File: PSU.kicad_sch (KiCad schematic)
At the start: 34 parts

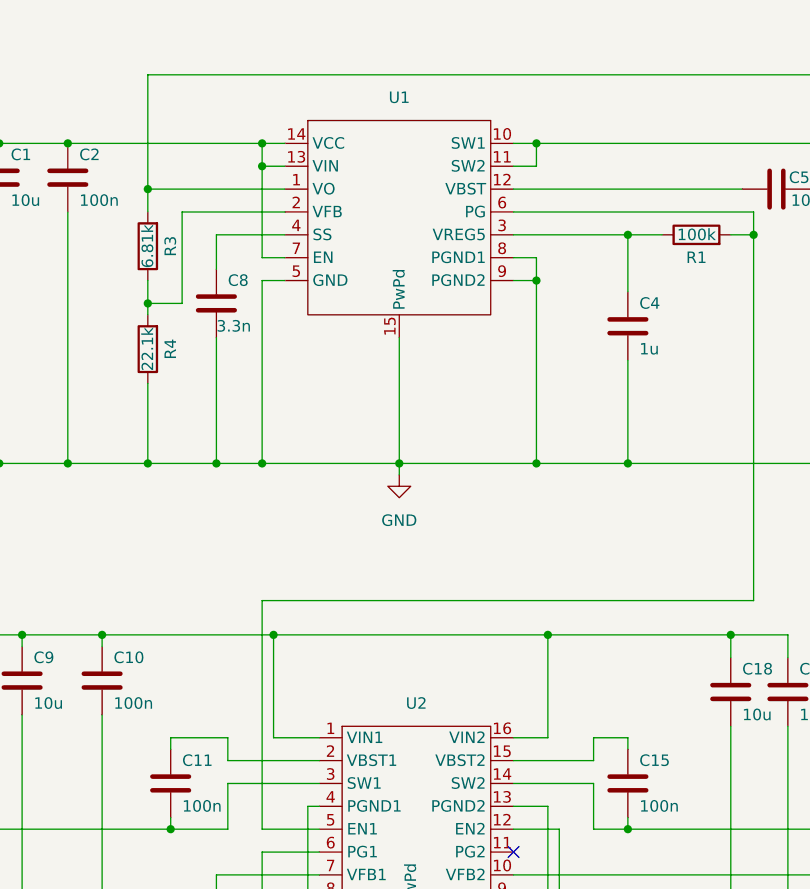
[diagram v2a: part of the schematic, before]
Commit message: Now follows with Electrical Rules
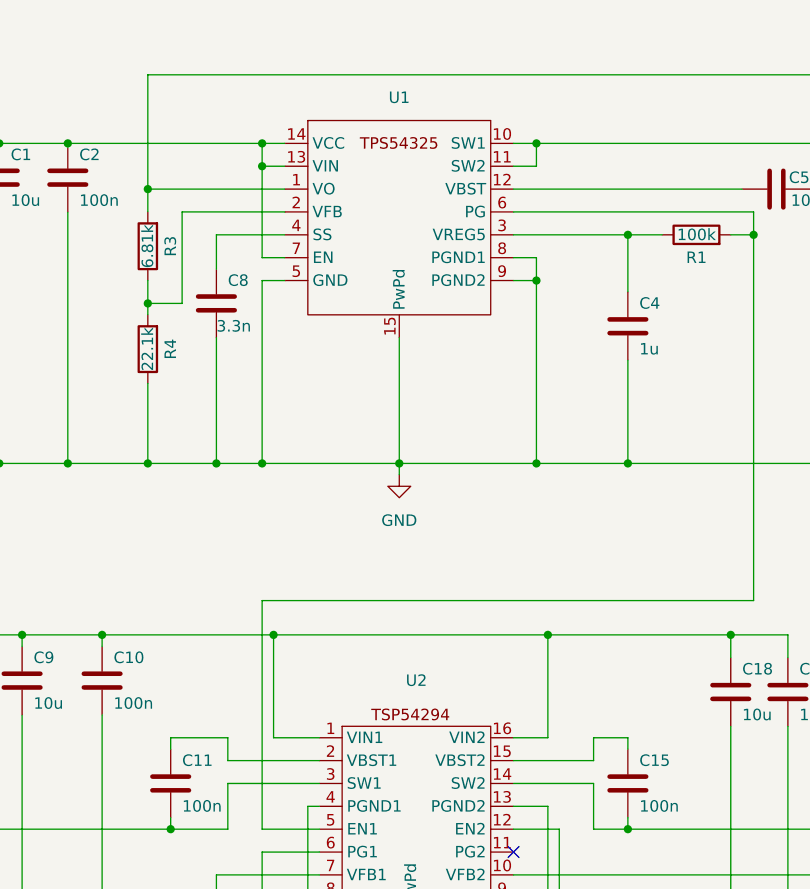
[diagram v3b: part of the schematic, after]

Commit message: Added footprints to symbols
Some nice light work
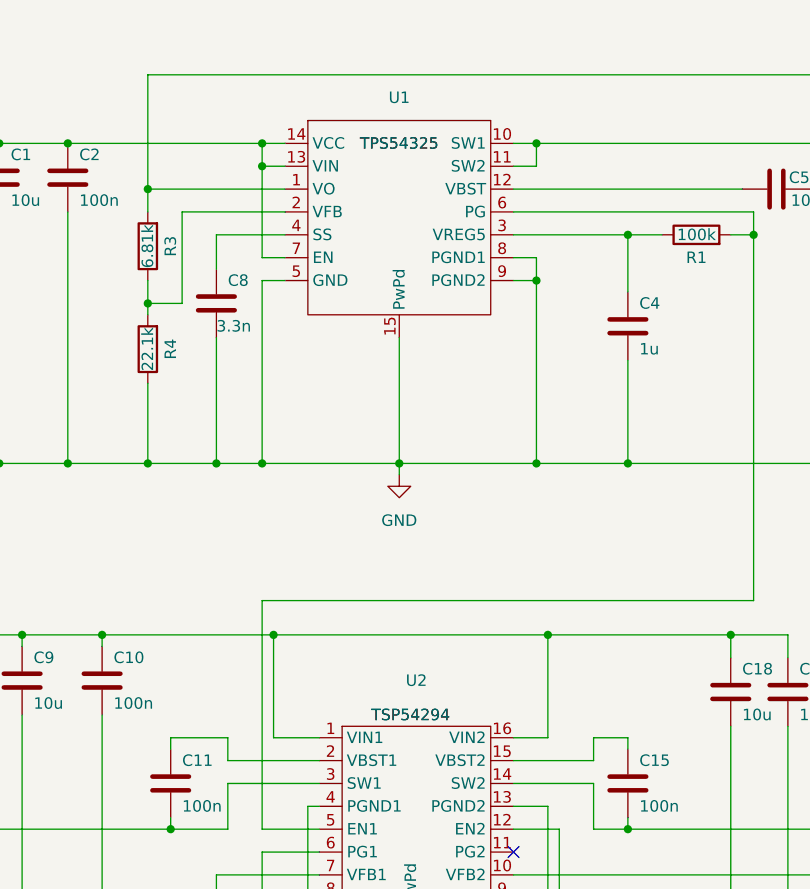
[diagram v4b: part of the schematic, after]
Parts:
- C1, C10, C11, C12, C13, C14, C15, C16, C17, C18, C19, C2, C3, C4, C5, C6, C7, C8, C9: footprint (none) -> Capacitor_SMD:C_1206_3216Metric
- FB1: footprint (none) -> Inductor_SMD:L_0603_1608Metric
- L1, L2, L3: footprint (none) -> Inductor_SMD:L_0805_2012Metric
- R1, R2, R3, R4, R5, R6, R7, R8, R9: footprint (none) -> Resistor_SMD:R_1206_3216Metric
- U1: value ~ -> TPS54325; footprint (none) -> Package_SO:TSSOP-14-1EP_4.4x5mm_P0.65mm
- U2: value ~ -> TSP54294; footprint (none) -> Package_SO:HTSSOP-16-1EP_4.4x5mm_P0.65mm_EP3x3mm
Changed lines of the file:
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@@
       (effects (font (size 1.27 1.27)))
     )
-    (property "Footprint" "" (at 101.6 130.81 0)
+    (property "Footprint" "Inductor_SMD:L_0805_2012Metric" (at 101.6 130.81 0)
       (effects (font (size 1.27 1.27)) hide)
     )
@@
       (effects (font (size 1.27 1.27)) (justify left))
     )
-    (property "Footprint" "" (at 180.0352 129.54 0)
+    (property "Footprint" "Capacitor_SMD:C_1206_3216Metric" (at 180.0352 129.54 0)
       (effects (font (size 1.27 1.27)) hide)
     )
@@
       (effects (font (size 1.27 1.27)))
     )
-    (property "Footprint" "" (at 237.998 146.05 90)
+    (property "Footprint" "Resistor_SMD:R_1206_3216Metric" (at 237.998 146.05 90)
       (effects (font (size 1.27 1.27)) hide)
     )
@@
       (effects (font (size 1.27 1.27)) (justify left))
     )
-    (property "Footprint" "" (at 93.6752 139.7 0)
+    (property "Footprint" "Capacitor_SMD:C_1206_3216Metric" (at 93.6752 139.7 0)
       (effects (font (size 1.27 1.27)) hide)
     )
@@
       (effects (font (size 1.27 1.27)) (justify left))
     )
-    (property "Footprint" "" (at 216.8652 66.04 0)
+    (property "Footprint" "Capacitor_SMD:C_1206_3216Metric" (at 216.8652 66.04 0)
       (effects (font (size 1.27 1.27)) hide)
     )
@@
       (effects (font (size 1.27 1.27)) (justify left))
     )
-    (property "Footprint" "" (at 227.0252 139.7 0)
+    (property "Footprint" "Capacitor_SMD:C_1206_3216Metric" (at 227.0252 139.7 0)
       (effects (font (size 1.27 1.27)) hide)
     )
@@
       (effects (font (size 1.27 1.27)) (justify left))
     )
-    (property "Footprint" "" (at 134.3152 76.2 0)
+    (property "Footprint" "Capacitor_SMD:C_1206_3216Metric" (at 134.3152 76.2 0)
       (effects (font (size 1.27 1.27)) hide)
     )
@@
       (effects (font (size 1.27 1.27)) (justify left))
     )
-    (property "Footprint" "" (at 191.4652 119.38 0)
+    (property "Footprint" "Capacitor_SMD:C_1206_3216Metric" (at 191.4652 119.38 0)
       (effects (font (size 1.27 1.27)) hide)
     )
@@
       (effects (font (size 1.27 1.27)))
     )
-    (property "Footprint" "" (at 237.998 135.89 90)
+    (property "Footprint" "Resistor_SMD:R_1206_3216Metric" (at 237.998 135.89 90)
       (effects (font (size 1.27 1.27)) hide)
     )
@@
       (effects (font (size 1.27 1.27)) (justify left))
     )
-    (property "Footprint" "" (at 180.0352 78.74 0)
+    (property "Footprint" "Capacitor_SMD:C_1206_3216Metric" (at 180.0352 78.74 0)
       (effects (font (size 1.27 1.27)) hide)
     )
@@
       (effects (font (size 1.27 1.27)))
     )
-    (property "Footprint" "" (at 127.508 77.47 90)
+    (property "Footprint" "Resistor_SMD:R_1206_3216Metric" (at 127.508 77.47 90)
       (effects (font (size 1.27 1.27)) hide)
     )
@@
       (effects (font (size 1.27 1.27)) (justify left))
     )
-    (property "Footprint" "" (at 117.8052 62.23 0)
+    (property "Footprint" "Capacitor_SMD:C_1206_3216Metric" (at 117.8052 62.23 0)
       (effects (font (size 1.27 1.27)) hide)
     )
@@
       (effects (font (size 1.27 1.27)) (justify left))
     )
-    (property "Footprint" "" (at 112.7252 118.11 0)
+    (property "Footprint" "Capacitor_SMD:C_1206_3216Metric" (at 112.7252 118.11 0)
       (effects (font (size 1.27 1.27)) hide)
     )
@@
       (effects (font (size 1.27 1.27)) (justify left))
     )
-    (property "Footprint" "" (at 129.2352 129.54 0)
+    (property "Footprint" "Capacitor_SMD:C_1206_3216Metric" (at 129.2352 129.54 0)
       (effects (font (size 1.27 1.27)) hide)
     )
@@
       (effects (font (size 1.27 1.27)))
     )
-    (property "Footprint" "" (at 208.28 54.61 0)
+    (property "Footprint" "Inductor_SMD:L_0805_2012Metric" (at 208.28 54.61 0)
       (effects (font (size 1.27 1.27)) hide)
     )
@@
   )
   (symbol (lib_id "GuitarZero:TPS54294") (at 154.94 129.54 0) (unit 1)
-    (in_bom yes) (on_board yes) (dnp no) (fields_autoplaced)
+    (in_bom yes) (on_board yes) (dnp no)
     (property "Reference" "U2" (at 155.575 114.3 0)
       (effects (font (size 1.27 1.27)))
     )
-    (property "Value" "~" (at 154.94 116.84 0)
-      (effects (font (size 1.27 1.27)))
-    )
-    (property "Footprint" "" (at 154.94 116.84 0)
+    (property "Value" "TSP54294" (at 154.94 118.11 0)
+      (effects (font (size 1.27 1.27)))
+    )
+    (property "Footprint" "Package_SO:HTSSOP-16-1EP_4.4x5mm_P0.65mm_EP3x3mm" (at 154.94 116.84 0)
       (effects (font (size 1.27 1.27)) hide)
     )
@@
       (effects (font (size 1.27 1.27)) (justify left))
     )
-    (property "Footprint" "" (at 219.4052 139.7 0)
+    (property "Footprint" "Capacitor_SMD:C_1206_3216Metric" (at 219.4052 139.7 0)
       (effects (font (size 1.27 1.27)) hide)
     )
@@
       (effects (font (size 1.27 1.27)))
     )
-    (property "Footprint" "" (at 186.69 66.548 90)
+    (property "Footprint" "Resistor_SMD:R_1206_3216Metric" (at 186.69 66.548 90)
       (effects (font (size 1.27 1.27)) hide)
     )
@@
       (effects (font (size 1.27 1.27)) (justify left))
     )
-    (property "Footprint" "" (at 121.6152 118.11 0)
+    (property "Footprint" "Capacitor_SMD:C_1206_3216Metric" (at 121.6152 118.11 0)
       (effects (font (size 1.27 1.27)) hide)
     )
@@
       (effects (font (size 1.27 1.27)) (justify left))
     )
-    (property "Footprint" "" (at 178.7652 147.32 0)
+    (property "Footprint" "Capacitor_SMD:C_1206_3216Metric" (at 178.7652 147.32 0)
       (effects (font (size 1.27 1.27)) hide)
     )
@@
   )
   (symbol (lib_id "GuitarZero:TPS54325") (at 153.67 62.23 0) (unit 1)
-    (in_bom yes) (on_board yes) (dnp no) (fields_autoplaced)
+    (in_bom yes) (on_board yes) (dnp no)
     (property "Reference" "U1" (at 153.67 49.53 0)
       (effects (font (size 1.27 1.27)))
     )
-    (property "Value" "~" (at 153.67 62.23 0)
-      (effects (font (size 1.27 1.27)))
-    )
-    (property "Footprint" "" (at 153.67 62.23 0)
+    (property "Value" "TPS54325" (at 153.67 54.61 0)
+      (effects (font (size 1.27 1.27)))
+    )
+    (property "Footprint" "Package_SO:TSSOP-14-1EP_4.4x5mm_P0.65mm" (at 153.67 62.23 0)
       (effects (font (size 1.27 1.27)) hide)
     )
@@
       (effects (font (size 1.27 1.27)))
     )
-    (property "Footprint" "" (at 72.898 146.05 90)
+    (property "Footprint" "Resistor_SMD:R_1206_3216Metric" (at 72.898 146.05 90)
       (effects (font (size 1.27 1.27)) hide)
     )
@@
       (effects (font (size 1.27 1.27)) (justify left))
     )
-    (property "Footprint" "" (at 101.6 58.42 0)
+    (property "Footprint" "Capacitor_SMD:C_1206_3216Metric" (at 101.6 58.42 0)
       (effects (font (size 1.27 1.27)) hide)
     )
@@
       (effects (font (size 1.27 1.27)) (justify left))
     )
-    (property "Footprint" "" (at 197.8152 119.38 0)
+    (property "Footprint" "Capacitor_SMD:C_1206_3216Metric" (at 197.8152 119.38 0)
       (effects (font (size 1.27 1.27)) hide)
     )
@@
       (effects (font (size 1.27 1.27)))
     )
-    (property "Footprint" "" (at 208.28 130.81 0)
+    (property "Footprint" "Inductor_SMD:L_0805_2012Metric" (at 208.28 130.81 0)
       (effects (font (size 1.27 1.27)) hide)
     )
@@
       (effects (font (size 1.27 1.27)) (justify left))
     )
-    (property "Footprint" "" (at 225.7552 66.04 0)
+    (property "Footprint" "Capacitor_SMD:C_1206_3216Metric" (at 225.7552 66.04 0)
       (effects (font (size 1.27 1.27)) hide)
     )
@@
       (effects (font (size 1.27 1.27)))
     )
-    (property "Footprint" "" (at 259.08 129.032 90)
+    (property "Footprint" "Resistor_SMD:R_1206_3216Metric" (at 259.08 129.032 90)
       (effects (font (size 1.27 1.27)) hide)
     )
@@
       (effects (font (size 1.27 1.27)))
     )
-    (property "Footprint" "" (at 251.46 132.588 90)
+    (property "Footprint" "Inductor_SMD:L_0603_1608Metric" (at 251.46 132.588 90)
       (effects (font (size 1.27 1.27)) hide)
     )
@@
       (effects (font (size 1.27 1.27)))
     )
-    (property "Footprint" "" (at 191.77 60.6552 0)
+    (property "Footprint" "Capacitor_SMD:C_1206_3216Metric" (at 191.77 60.6552 0)
       (effects (font (size 1.27 1.27)) hide)
     )
@@
       (effects (font (size 1.27 1.27)))
     )
-    (property "Footprint" "" (at 188.468 143.51 90)
+    (property "Footprint" "Resistor_SMD:R_1206_3216Metric" (at 188.468 143.51 90)
       (effects (font (size 1.27 1.27)) hide)
     )
@@
       (effects (font (size 1.27 1.27)))
     )
-    (property "Footprint" "" (at 72.898 135.89 90)
+    (property "Footprint" "Resistor_SMD:R_1206_3216Metric" (at 72.898 135.89 90)
       (effects (font (size 1.27 1.27)) hide)
     )
@@
       (effects (font (size 1.27 1.27)))
     )
-    (property "Footprint" "" (at 127.508 66.04 90)
+    (property "Footprint" "Resistor_SMD:R_1206_3216Metric" (at 127.508 66.04 90)
       (effects (font (size 1.27 1.27)) hide)
     )
@@
       (effects (font (size 1.27 1.27)) (justify left))
     )
-    (property "Footprint" "" (at 110.1852 62.23 0)
+    (property "Footprint" "Capacitor_SMD:C_1206_3216Metric" (at 110.1852 62.23 0)
       (effects (font (size 1.27 1.27)) hide)
     )
@@
       (effects (font (size 1.27 1.27)) (justify left))
     )
-    (property "Footprint" "" (at 83.5152 139.7 0)
-      (effects (font (size 1.27 1.27)) hide)
-    )
+    (property "Footprint" "Capacitor_SMD:C_1206_3216Metric" (at 83.5152 139.7 0)
+      (effects (font (size 1.27 1.27)) hide)
+    )

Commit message: Changed Reistor and Capacitor size fomr 1206 to 0805
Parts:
- C1, C10, C11, C12, C13, C14, C15, C16, C17, C18, C19, C2, C3, C4, C5, C6, C7, C8, C9: footprint Capacitor_SMD:C_1206_3216Metric -> Capacitor_SMD:C_0805_2012Metric
- R1, R2, R3, R4, R5, R6, R7, R8, R9: footprint Resistor_SMD:R_1206_3216Metric -> Resistor_SMD:R_0805_2012Metric
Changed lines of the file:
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@@
       (effects (font (size 1.27 1.27)) (justify left))
     )
-    (property "Footprint" "Capacitor_SMD:C_1206_3216Metric" (at 180.0352 129.54 0)
+    (property "Footprint" "Capacitor_SMD:C_0805_2012Metric" (at 180.0352 129.54 0)
       (effects (font (size 1.27 1.27)) hide)
     )
@@
       (effects (font (size 1.27 1.27)))
     )
-    (property "Footprint" "Resistor_SMD:R_1206_3216Metric" (at 237.998 146.05 90)
+    (property "Footprint" "Resistor_SMD:R_0805_2012Metric" (at 237.998 146.05 90)
       (effects (font (size 1.27 1.27)) hide)
     )
@@
       (effects (font (size 1.27 1.27)) (justify left))
     )
-    (property "Footprint" "Capacitor_SMD:C_1206_3216Metric" (at 93.6752 139.7 0)
+    (property "Footprint" "Capacitor_SMD:C_0805_2012Metric" (at 93.6752 139.7 0)
       (effects (font (size 1.27 1.27)) hide)
     )
@@
       (effects (font (size 1.27 1.27)) (justify left))
     )
-    (property "Footprint" "Capacitor_SMD:C_1206_3216Metric" (at 216.8652 66.04 0)
+    (property "Footprint" "Capacitor_SMD:C_0805_2012Metric" (at 216.8652 66.04 0)
       (effects (font (size 1.27 1.27)) hide)
     )
@@
       (effects (font (size 1.27 1.27)) (justify left))
     )
-    (property "Footprint" "Capacitor_SMD:C_1206_3216Metric" (at 227.0252 139.7 0)
+    (property "Footprint" "Capacitor_SMD:C_0805_2012Metric" (at 227.0252 139.7 0)
       (effects (font (size 1.27 1.27)) hide)
     )
@@
       (effects (font (size 1.27 1.27)) (justify left))
     )
-    (property "Footprint" "Capacitor_SMD:C_1206_3216Metric" (at 134.3152 76.2 0)
+    (property "Footprint" "Capacitor_SMD:C_0805_2012Metric" (at 134.3152 76.2 0)
       (effects (font (size 1.27 1.27)) hide)
     )
@@
       (effects (font (size 1.27 1.27)) (justify left))
     )
-    (property "Footprint" "Capacitor_SMD:C_1206_3216Metric" (at 191.4652 119.38 0)
+    (property "Footprint" "Capacitor_SMD:C_0805_2012Metric" (at 191.4652 119.38 0)
       (effects (font (size 1.27 1.27)) hide)
     )
@@
       (effects (font (size 1.27 1.27)))
     )
-    (property "Footprint" "Resistor_SMD:R_1206_3216Metric" (at 237.998 135.89 90)
+    (property "Footprint" "Resistor_SMD:R_0805_2012Metric" (at 237.998 135.89 90)
       (effects (font (size 1.27 1.27)) hide)
     )
@@
       (effects (font (size 1.27 1.27)) (justify left))
     )
-    (property "Footprint" "Capacitor_SMD:C_1206_3216Metric" (at 180.0352 78.74 0)
+    (property "Footprint" "Capacitor_SMD:C_0805_2012Metric" (at 180.0352 78.74 0)
       (effects (font (size 1.27 1.27)) hide)
     )
@@
       (effects (font (size 1.27 1.27)))
     )
-    (property "Footprint" "Resistor_SMD:R_1206_3216Metric" (at 127.508 77.47 90)
+    (property "Footprint" "Resistor_SMD:R_0805_2012Metric" (at 127.508 77.47 90)
       (effects (font (size 1.27 1.27)) hide)
     )
@@
       (effects (font (size 1.27 1.27)) (justify left))
     )
-    (property "Footprint" "Capacitor_SMD:C_1206_3216Metric" (at 117.8052 62.23 0)
+    (property "Footprint" "Capacitor_SMD:C_0805_2012Metric" (at 117.8052 62.23 0)
       (effects (font (size 1.27 1.27)) hide)
     )
@@
       (effects (font (size 1.27 1.27)) (justify left))
     )
-    (property "Footprint" "Capacitor_SMD:C_1206_3216Metric" (at 112.7252 118.11 0)
+    (property "Footprint" "Capacitor_SMD:C_0805_2012Metric" (at 112.7252 118.11 0)
       (effects (font (size 1.27 1.27)) hide)
     )
@@
       (effects (font (size 1.27 1.27)) (justify left))
     )
-    (property "Footprint" "Capacitor_SMD:C_1206_3216Metric" (at 129.2352 129.54 0)
+    (property "Footprint" "Capacitor_SMD:C_0805_2012Metric" (at 129.2352 129.54 0)
       (effects (font (size 1.27 1.27)) hide)
     )
@@
       (effects (font (size 1.27 1.27)) (justify left))
     )
-    (property "Footprint" "Capacitor_SMD:C_1206_3216Metric" (at 219.4052 139.7 0)
+    (property "Footprint" "Capacitor_SMD:C_0805_2012Metric" (at 219.4052 139.7 0)
       (effects (font (size 1.27 1.27)) hide)
     )
@@
       (effects (font (size 1.27 1.27)))
     )
-    (property "Footprint" "Resistor_SMD:R_1206_3216Metric" (at 186.69 66.548 90)
+    (property "Footprint" "Resistor_SMD:R_0805_2012Metric" (at 186.69 66.548 90)
       (effects (font (size 1.27 1.27)) hide)
     )
@@
       (effects (font (size 1.27 1.27)) (justify left))
     )
-    (property "Footprint" "Capacitor_SMD:C_1206_3216Metric" (at 121.6152 118.11 0)
+    (property "Footprint" "Capacitor_SMD:C_0805_2012Metric" (at 121.6152 118.11 0)
       (effects (font (size 1.27 1.27)) hide)
     )
@@
       (effects (font (size 1.27 1.27)) (justify left))
     )
-    (property "Footprint" "Capacitor_SMD:C_1206_3216Metric" (at 178.7652 147.32 0)
+    (property "Footprint" "Capacitor_SMD:C_0805_2012Metric" (at 178.7652 147.32 0)
       (effects (font (size 1.27 1.27)) hide)
     )
@@
       (effects (font (size 1.27 1.27)))
     )
-    (property "Footprint" "Resistor_SMD:R_1206_3216Metric" (at 72.898 146.05 90)
+    (property "Footprint" "Resistor_SMD:R_0805_2012Metric" (at 72.898 146.05 90)
       (effects (font (size 1.27 1.27)) hide)
     )
@@
       (effects (font (size 1.27 1.27)) (justify left))
     )
-    (property "Footprint" "Capacitor_SMD:C_1206_3216Metric" (at 101.6 58.42 0)
+    (property "Footprint" "Capacitor_SMD:C_0805_2012Metric" (at 101.6 58.42 0)
       (effects (font (size 1.27 1.27)) hide)
     )
@@
       (effects (font (size 1.27 1.27)) (justify left))
     )
-    (property "Footprint" "Capacitor_SMD:C_1206_3216Metric" (at 197.8152 119.38 0)
+    (property "Footprint" "Capacitor_SMD:C_0805_2012Metric" (at 197.8152 119.38 0)
       (effects (font (size 1.27 1.27)) hide)
     )
@@
       (effects (font (size 1.27 1.27)) (justify left))
     )
-    (property "Footprint" "Capacitor_SMD:C_1206_3216Metric" (at 225.7552 66.04 0)
+    (property "Footprint" "Capacitor_SMD:C_0805_2012Metric" (at 225.7552 66.04 0)
       (effects (font (size 1.27 1.27)) hide)
     )
@@
       (effects (font (size 1.27 1.27)))
     )
-    (property "Footprint" "Resistor_SMD:R_1206_3216Metric" (at 259.08 129.032 90)
+    (property "Footprint" "Resistor_SMD:R_0805_2012Metric" (at 259.08 129.032 90)
       (effects (font (size 1.27 1.27)) hide)
     )
@@
       (effects (font (size 1.27 1.27)))
     )
-    (property "Footprint" "Capacitor_SMD:C_1206_3216Metric" (at 191.77 60.6552 0)
+    (property "Footprint" "Capacitor_SMD:C_0805_2012Metric" (at 191.77 60.6552 0)
       (effects (font (size 1.27 1.27)) hide)
     )
@@
       (effects (font (size 1.27 1.27)))
     )
-    (property "Footprint" "Resistor_SMD:R_1206_3216Metric" (at 188.468 143.51 90)
+    (property "Footprint" "Resistor_SMD:R_0805_2012Metric" (at 188.468 143.51 90)
       (effects (font (size 1.27 1.27)) hide)
     )
@@
       (effects (font (size 1.27 1.27)))
     )
-    (property "Footprint" "Resistor_SMD:R_1206_3216Metric" (at 72.898 135.89 90)
+    (property "Footprint" "Resistor_SMD:R_0805_2012Metric" (at 72.898 135.89 90)
       (effects (font (size 1.27 1.27)) hide)
     )
@@
       (effects (font (size 1.27 1.27)))
     )
-    (property "Footprint" "Resistor_SMD:R_1206_3216Metric" (at 127.508 66.04 90)
+    (property "Footprint" "Resistor_SMD:R_0805_2012Metric" (at 127.508 66.04 90)
       (effects (font (size 1.27 1.27)) hide)
     )
@@
       (effects (font (size 1.27 1.27)) (justify left))
     )
-    (property "Footprint" "Capacitor_SMD:C_1206_3216Metric" (at 110.1852 62.23 0)
+    (property "Footprint" "Capacitor_SMD:C_0805_2012Metric" (at 110.1852 62.23 0)
       (effects (font (size 1.27 1.27)) hide)
     )
@@
       (effects (font (size 1.27 1.27)) (justify left))
     )
-    (property "Footprint" "Capacitor_SMD:C_1206_3216Metric" (at 83.5152 139.7 0)
-      (effects (font (size 1.27 1.27)) hide)
-    )
+    (property "Footprint" "Capacitor_SMD:C_0805_2012Metric" (at 83.5152 139.7 0)
+      (effects (font (size 1.27 1.27)) hide)
+    )
